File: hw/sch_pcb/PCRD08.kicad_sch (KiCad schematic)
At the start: 8 parts, among them M101 HOLE, M102 HOLE, M103 HOLE, M104 HOLE

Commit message: Add files via upload
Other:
- note added: "pls zkontrolovat ze R208, R207, R206 a C213 maji spravne hodnoty aby to neinvertovalo a melo 1x gain pro vysoke frekvence, dekuji"
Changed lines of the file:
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@@
 		(comment 4 "GPL 3")
+	)
+	(text "pls zkontrolovat ze R208, R207, R206 a C213\nmaji spravne hodnoty aby to neinvertovalo a \nmelo 1x gain pro vysoke frekvence, dekuji "
+		(exclude_from_sim no)
+		(at 108.204 66.04 0)
+		(effects
+			(font
+				(size 1.524 1.524)
+			)
+		)
 	)
 	(text "MOUNTING HOLES"

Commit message: Rename project PCRD008 -> PCRD08 to match MLAB module naming convention
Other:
- title: PCRD008 -> PCRD08
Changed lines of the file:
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@@
 	(paper "A4")
 	(title_block
-		(title "PCRD008")
+		(title "PCRD08")
 		(date "2026-07-24")
 		(company "KubFire <info@ust.cz>")
@@
 		)
 		(instances
-			(project "PCRD008"
+			(project "PCRD08"
 				(path "/e63e39d7-6ac0-4ffd-8aa3-1841a4541b55"
 					(page "2")
@@
 		)
 		(instances
-			(project "PCRD008"
+			(project "PCRD08"
 				(path "/e63e39d7-6ac0-4ffd-8aa3-1841a4541b55"
 					(page "1")

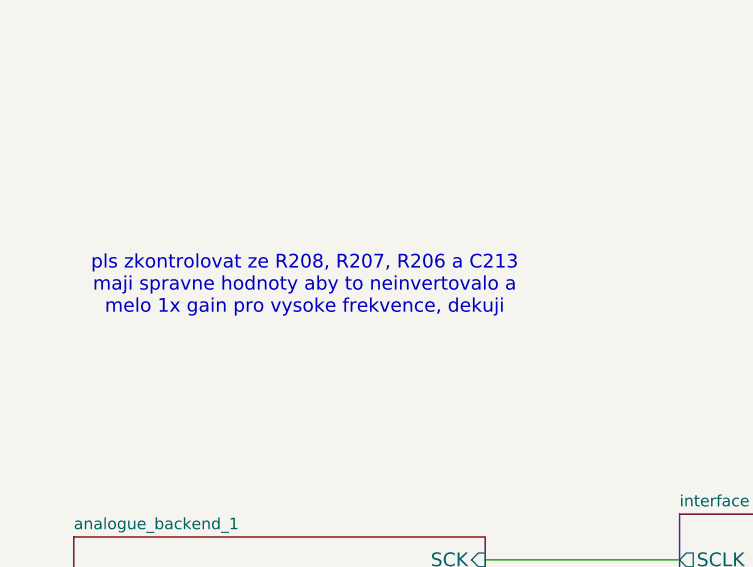
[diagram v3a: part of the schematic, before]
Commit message: Remove resolved TODO notes on R206/R207/R208/C213 gain check
Verified U201 AC-coupled non-inverting stage: signal path enters the
+ input via C211, so it cannot invert, and the R206/R207/R208/C213
network algebraically settles to unity gain at high frequency
regardless of exact values (confirmed numerically with the populated
values: phase stays within ±90°, |H|→1 above ~10 MHz).
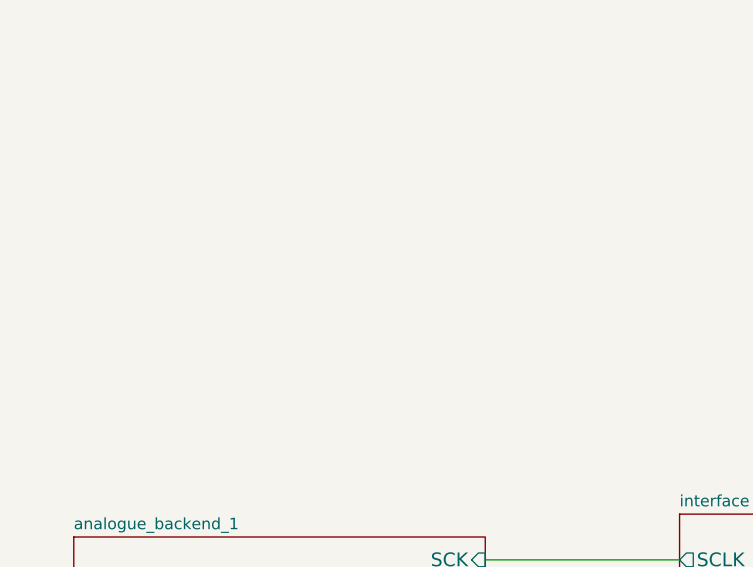
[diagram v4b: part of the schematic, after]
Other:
- note removed: "pls zkontrolovat ze R208, R207, R206 a C213 maji spravne hodnoty aby to neinvertovalo a melo 1x gain pro vysoke frekvence, dekuji"
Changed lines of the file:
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@@
 		(comment 4 "GPL 3")
-	)
-	(text "pls zkontrolovat ze R208, R207, R206 a C213\nmaji spravne hodnoty aby to neinvertovalo a \nmelo 1x gain pro vysoke frekvence, dekuji "
-		(exclude_from_sim no)
-		(at 108.204 66.04 0)
-		(effects
-			(font
-				(size 1.524 1.524)
-			)
-		)
 	)
 	(text "MOUNTING HOLES"

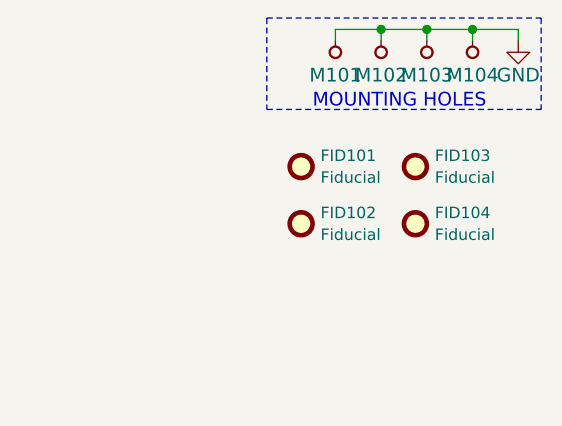
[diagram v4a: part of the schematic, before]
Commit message: Re-anotate schematics.
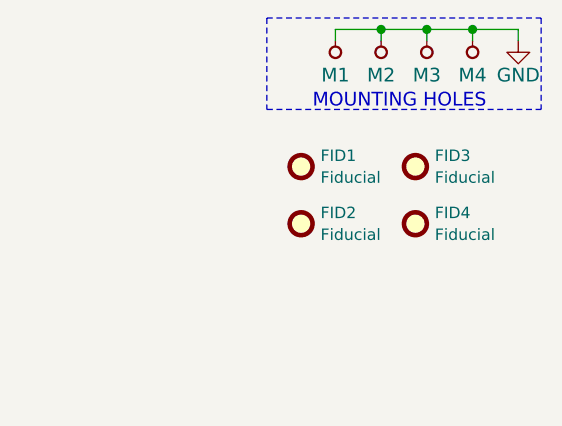
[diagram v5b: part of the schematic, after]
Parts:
- renumbered FID101 to FID1, FID102 to FID2, FID103 to FID3, FID104 to FID4, M101 to M1, M102 to M2, M103 to M3, M104 to M4
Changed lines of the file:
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@@
 		(in_pos_files yes)
 		(dnp no)
-		(property "Reference" "M101"
+		(property "Reference" "M1"
 			(at 255.27 26.67 90)
 			(show_name no)
@@
 			(project "PCRD08"
 				(path "/e63e39d7-6ac0-4ffd-8aa3-1841a4541b55"
-					(reference "M101")
+					(reference "M1")
 					(unit 1)
 				)
@@
 		(dnp no)
 		(fields_autoplaced yes)
-		(property "Reference" "FID104"
+		(property "Reference" "FID4"
 			(at 266.319 41.9679 0)
 			(show_name no)
@@
 			(project "PCRD08"
 				(path "/e63e39d7-6ac0-4ffd-8aa3-1841a4541b55"
-					(reference "FID104")
+					(reference "FID4")
 					(unit 1)
 				)
@@
 		(dnp no)
 		(fields_autoplaced yes)
-		(property "Reference" "FID102"
+		(property "Reference" "FID2"
 			(at 253.619 41.9679 0)
 			(show_name no)
@@
 			(project "PCRD08"
 				(path "/e63e39d7-6ac0-4ffd-8aa3-1841a4541b55"
-					(reference "FID102")
+					(reference "FID2")
 					(unit 1)
 				)
@@
 		(in_pos_files yes)
 		(dnp no)
-		(property "Reference" "#PWR0101"
+		(property "Reference" "#PWR01"
 			(at 275.59 29.21 0)
 			(hide yes)
@@
 			(project "PCRD08"
 				(path "/e63e39d7-6ac0-4ffd-8aa3-1841a4541b55"
-					(reference "#PWR0101")
+					(reference "#PWR01")
 					(unit 1)
 				)
@@
 		(in_pos_files yes)
 		(dnp no)
-		(property "Reference" "M102"
+		(property "Reference" "M2"
 			(at 260.35 26.67 90)
 			(show_name no)
@@
 			(project "PCRD08"
 				(path "/e63e39d7-6ac0-4ffd-8aa3-1841a4541b55"
-					(reference "M102")
+					(reference "M2")
 					(unit 1)
 				)
@@
 		(in_pos_files yes)
 		(dnp no)
-		(property "Reference" "M103"
+		(property "Reference" "M3"
 			(at 265.43 26.67 90)
 			(show_name no)
@@
 			(project "PCRD08"
 				(path "/e63e39d7-6ac0-4ffd-8aa3-1841a4541b55"
-					(reference "M103")
+					(reference "M3")
 					(unit 1)
 				)
@@
 		(dnp no)
 		(fields_autoplaced yes)
-		(property "Reference" "FID101"
+		(property "Reference" "FID1"
 			(at 253.619 35.6179 0)
 			(show_name no)
@@
 			(project "PCRD08"
 				(path "/e63e39d7-6ac0-4ffd-8aa3-1841a4541b55"
-					(reference "FID101")
+					(reference "FID1")
 					(unit 1)
 				)
@@
 		(dnp no)
 		(fields_autoplaced yes)
-		(property "Reference" "FID103"
+		(property "Reference" "FID3"
 			(at 266.319 35.6179 0)
 			(show_name no)
@@
 			(project "PCRD08"
 				(path "/e63e39d7-6ac0-4ffd-8aa3-1841a4541b55"
-					(reference "FID103")
+					(reference "FID3")
 					(unit 1)
 				)
@@
 		(in_pos_files yes)
 		(dnp no)
-		(property "Reference" "M104"
+		(property "Reference" "M4"
 			(at 270.51 26.67 90)
 			(show_name no)
@@
 			(project "PCRD08"
 				(path "/e63e39d7-6ac0-4ffd-8aa3-1841a4541b55"
-					(reference "M104")
-					(unit 1)
-				)
+					(reference "M4")
+					(unit 1)
+				)
